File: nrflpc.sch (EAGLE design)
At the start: 71 parts, among them IC1 LPC1111/12/13/14-HVQFN33, IC2 LT1763CS8-3.3, IC3 LM3401, IC5 LM3401, IC6 LM3401, IC7 LM3401, IC8 78L05SMD, Q1 20MHz, Q2 MOSFET-PCHANNEL, Q3 MOSFET-PCHANNEL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

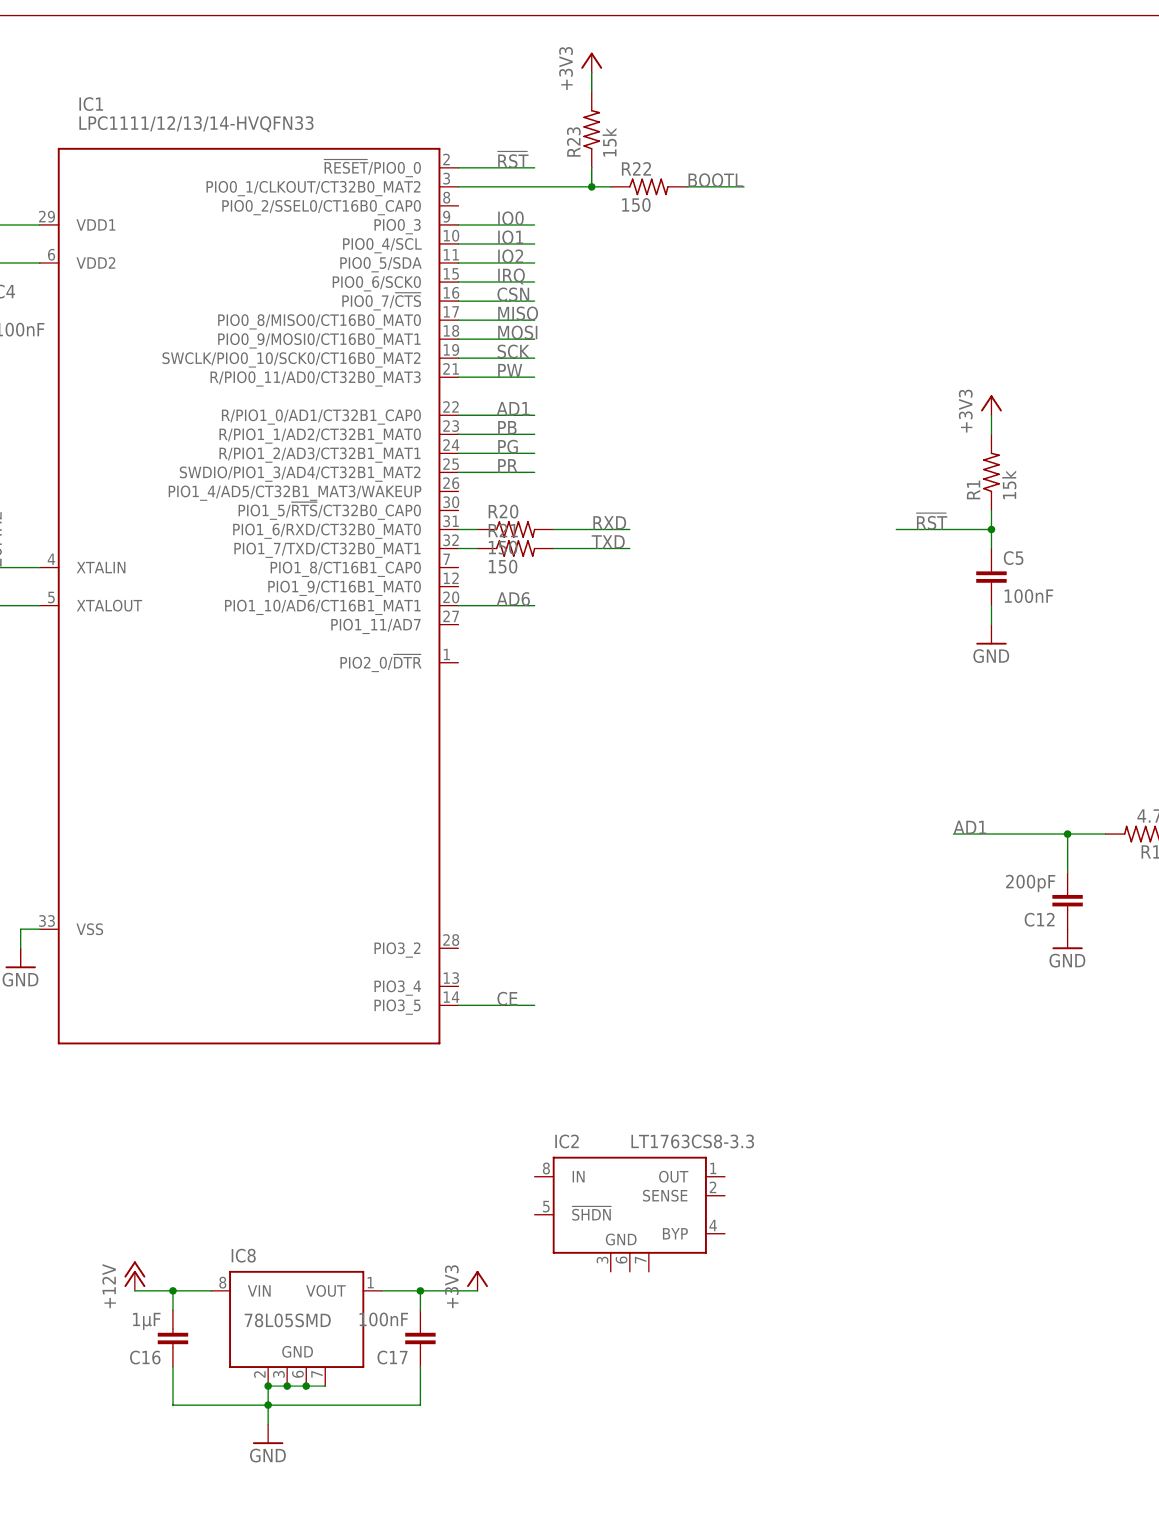
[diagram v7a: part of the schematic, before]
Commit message: Removed unnecessary pullups, new 3.3V regulator, begin routing
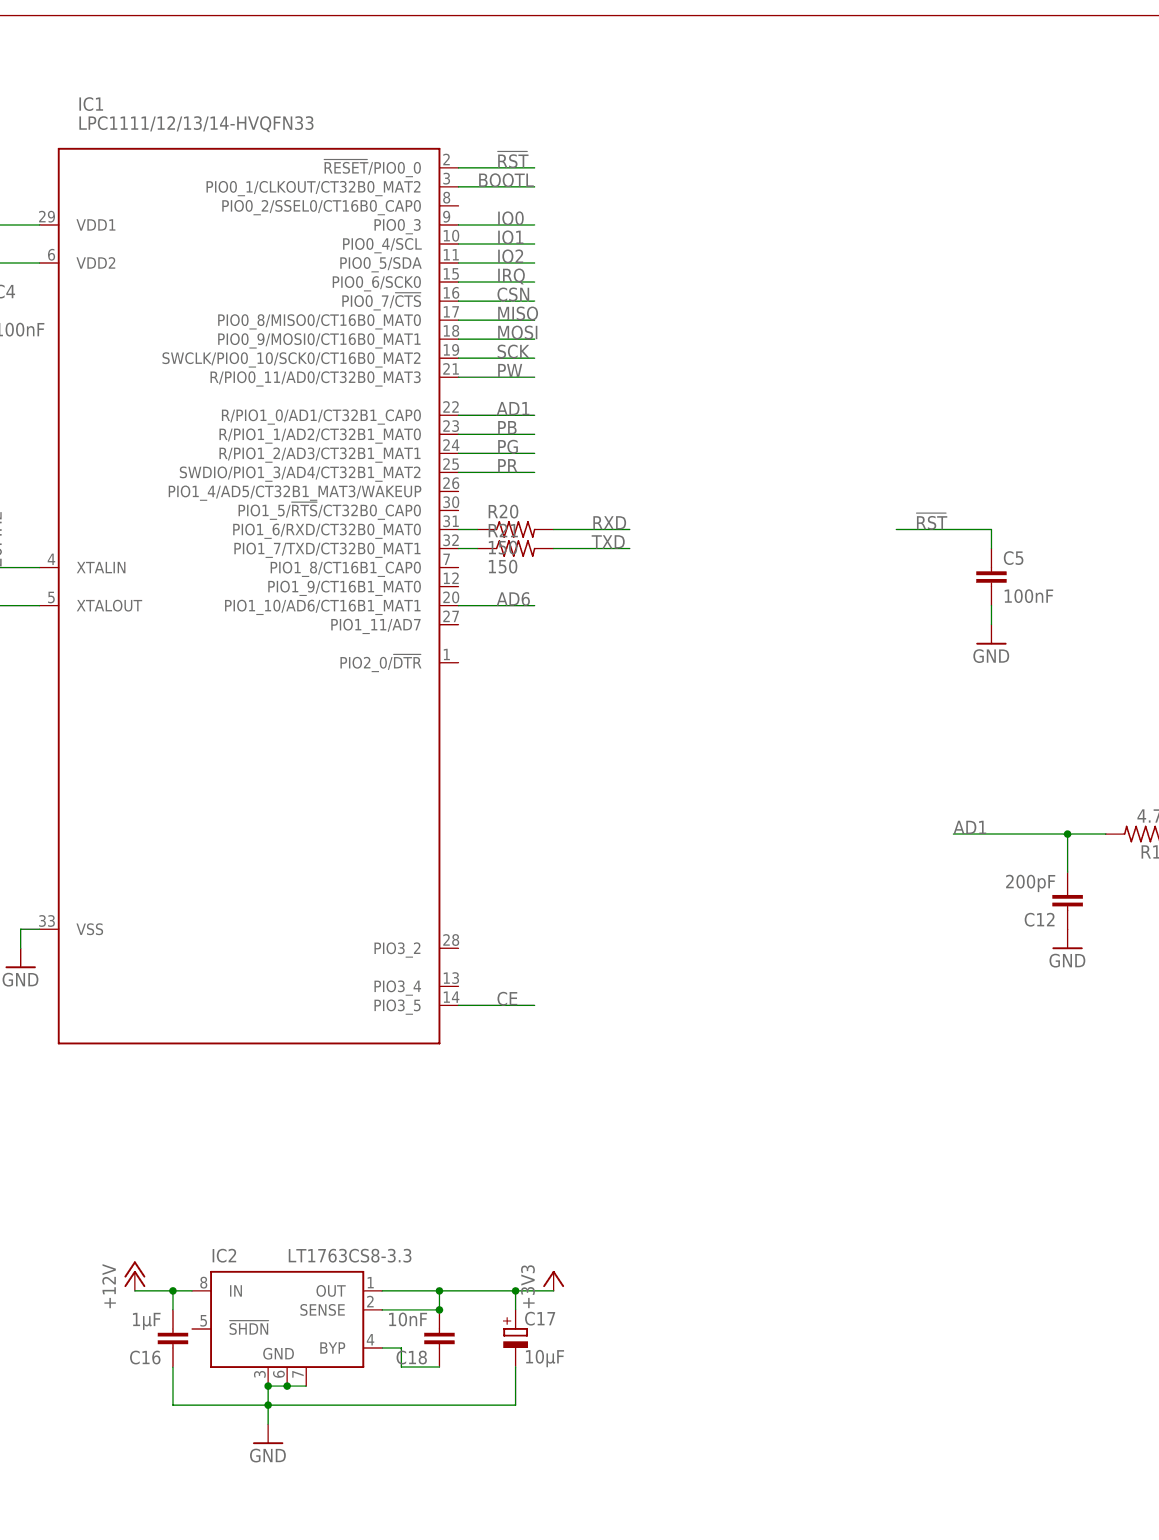
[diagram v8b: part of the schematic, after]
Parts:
- removed IC8: 78L05SMD, linear:78L05SMD
- removed R1, R23: 15k, rcl:R-US_R0402
- removed R22: 150, rcl:R-US_R0402
- added C18: 10nF, SparkFun:CAP0402-CAP
- C17: value 100nF -> 10µF; device SparkFun:CAP0402-CAP -> rcl:CPOL-EUSMCA
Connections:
- net !RST: no longer R1.1
- net +12V: now also IC2.IN; no longer IC8G$1.VIN
- net +3V3: now also C17.+, C18.2, IC2.OUT, IC2.SENSE; no longer C17.2, IC8G$1.VOUT, R1.2, R23.2
- net BOOTL: now also IC1.PIO0_1/CLKOUT/CT32B0_MAT2; no longer R22.2
- net GND: now also C17.-, IC2.GND@1, IC2.GND@2, IC2.GND@3; no longer C17.1, IC8G$1.GND@1, IC8G$1.GND@2, IC8G$1.GND@3, IC8G$1.GND@4
- net N$18: now also C18.1, IC2.BYP; no longer IC1.PIO0_1/CLKOUT/CT32B0_MAT2, R22.1, R23.1
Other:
- moved on the sheet: IC2
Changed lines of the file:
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@@
 <part name="B-" library="solpad" deviceset="SE14" device=""/>
 <part name="C15" library="SparkFun" deviceset="CAP" device="0805" value="1µF"/>
-<part name="IC8" library="linear" deviceset="78L*SMD" device="" technology="05"/>
 <part name="GND11" library="supply1" deviceset="GND" device=""/>
 <part name="C16" library="SparkFun" deviceset="CAP" device="0805" value="1µF"/>
-<part name="C17" library="SparkFun" deviceset="CAP" device="0402-CAP" value="100nF"/>
 <part name="+3V1" library="supply1" deviceset="+3V3" device=""/>
 <part name="FTDI" library="pinhead" deviceset="PINHD-1X4" device=""/>
@@
 <part name="C4" library="rcl" deviceset="C-EU" device="C0402" value="100nF"/>
 <part name="GND5" library="supply1" deviceset="GND" device=""/>
-<part name="R1" library="rcl" deviceset="R-US_" device="R0402" value="15k"/>
-<part name="+3V5" library="supply1" deviceset="+3V3" device=""/>
 <part name="GND13" library="supply1" deviceset="GND" device=""/>
 <part name="C5" library="rcl" deviceset="C-EU" device="C0402" value="100nF"/>
@@
 <part name="R21" library="rcl" deviceset="R-US_" device="R0402" value="150"/>
 <part name="IC2" library="linear-technology" deviceset="LT1763CS8" device="" technology="-3.3"/>
-<part name="R22" library="rcl" deviceset="R-US_" device="R0402" value="150"/>
-<part name="R23" library="rcl" deviceset="R-US_" device="R0402" value="15k"/>
-<part name="+3V3" library="supply1" deviceset="+3V3" device=""/>
+<part name="C18" library="SparkFun" deviceset="CAP" device="0402-CAP" value="10nF"/>
+<part name="C17" library="rcl" deviceset="CPOL-EU" device="SMCA" value="10µF"/>
 </parts>
 <sheets>
@@
 <instance part="B-" gate="1" x="398.78" y="-20.32" rot="R270"/>
 <instance part="C15" gate="G$1" x="396.24" y="-15.24" rot="R180"/>
-<instance part="IC8" gate="G$1" x="208.28" y="48.26"/>
 <instance part="GND11" gate="1" x="205.74" y="27.94"/>
 <instance part="C16" gate="G$1" x="193.04" y="43.18" rot="R180"/>
-<instance part="C17" gate="G$1" x="226.06" y="43.18" rot="R180"/>
-<instance part="+3V1" gate="G$1" x="233.68" y="50.8"/>
+<instance part="+3V1" gate="G$1" x="243.84" y="50.8"/>
 <instance part="FTDI" gate="A" x="88.9" y="139.7"/>
 <instance part="GND8" gate="1" x="73.66" y="134.62"/>
@@
 <instance part="C4" gate="G$1" x="167.64" y="180.34"/>
 <instance part="GND5" gate="1" x="162.56" y="170.18"/>
-<instance part="R1" gate="G$1" x="302.26" y="157.48" rot="R90"/>
-<instance part="+3V5" gate="G$1" x="302.26" y="167.64"/>
 <instance part="GND13" gate="1" x="302.26" y="134.62"/>
 <instance part="C5" gate="G$1" x="302.26" y="144.78"/>
@@
 <instance part="R20" gate="G$1" x="238.76" y="149.86"/>
 <instance part="R21" gate="G$1" x="238.76" y="147.32"/>
-<instance part="IC2" gate="G$1" x="254" y="60.96"/>
-<instance part="R22" gate="G$1" x="256.54" y="195.58"/>
-<instance part="R23" gate="G$1" x="248.92" y="203.2" rot="R90"/>
-<instance part="+3V3" gate="G$1" x="248.92" y="213.36"/>
+<instance part="IC2" gate="G$1" x="208.28" y="45.72"/>
+<instance part="C18" gate="G$1" x="228.6" y="43.18" rot="R180"/>
+<instance part="C17" gate="G$1" x="238.76" y="43.18"/>
 </instances>
 <busses>
@@
 </segment>
 <segment>
-<wire x1="213.36" y1="35.56" x2="210.82" y2="35.56" width="0.1524" layer="91"/>
-<wire x1="210.82" y1="35.56" x2="208.28" y2="35.56" width="0.1524" layer="91"/>
-<wire x1="208.28" y1="35.56" x2="205.74" y2="35.56" width="0.1524" layer="91"/>
-<wire x1="205.74" y1="35.56" x2="205.74" y2="33.02" width="0.1524" layer="91"/>
 <wire x1="205.74" y1="33.02" x2="205.74" y2="30.48" width="0.1524" layer="91"/>
-<wire x1="226.06" y1="38.1" x2="226.06" y2="33.02" width="0.1524" layer="91"/>
-<wire x1="226.06" y1="33.02" x2="205.74" y2="33.02" width="0.1524" layer="91"/>
 <wire x1="205.74" y1="33.02" x2="193.04" y2="33.02" width="0.1524" layer="91"/>
 <wire x1="193.04" y1="33.02" x2="193.04" y2="38.1" width="0.1524" layer="91"/>
-<junction x="210.82" y="35.56"/>
+<pinref part="GND11" gate="1" pin="GND"/>
+<pinref part="C16" gate="G$1" pin="1"/>
+<wire x1="238.76" y1="33.02" x2="205.74" y2="33.02" width="0.1524" layer="91"/>
+<junction x="205.74" y="33.02"/>
+<wire x1="238.76" y1="33.02" x2="238.76" y2="38.1" width="0.1524" layer="91"/>
+<pinref part="IC2" gate="G$1" pin="GND@1"/>
+<wire x1="205.74" y1="35.56" x2="205.74" y2="33.02" width="0.1524" layer="91"/>
+<pinref part="IC2" gate="G$1" pin="GND@2"/>
+<wire x1="205.74" y1="35.56" x2="208.28" y2="35.56" width="0.1524" layer="91"/>
+<junction x="205.74" y="35.56"/>
+<pinref part="IC2" gate="G$1" pin="GND@3"/>
+<wire x1="208.28" y1="35.56" x2="210.82" y2="35.56" width="0.1524" layer="91"/>
 <junction x="208.28" y="35.56"/>
-<junction x="205.74" y="35.56"/>
-<junction x="205.74" y="33.02"/>
-<pinref part="IC8" gate="G$1" pin="GND@4"/>
-<pinref part="IC8" gate="G$1" pin="GND@3"/>
-<pinref part="IC8" gate="G$1" pin="GND@2"/>
-<pinref part="IC8" gate="G$1" pin="GND@1"/>
-<pinref part="GND11" gate="1" pin="GND"/>
-<pinref part="C17" gate="G$1" pin="1"/>
-<pinref part="C16" gate="G$1" pin="1"/>
+<pinref part="C17" gate="G$1" pin="-"/>
 </segment>
 <segment>
@@
 </segment>
 <segment>
-<pinref part="R1" gate="G$1" pin="1"/>
 <pinref part="C5" gate="G$1" pin="1"/>
 <wire x1="302.26" y1="147.32" x2="302.26" y2="149.86" width="0.1524" layer="91"/>
-<wire x1="302.26" y1="149.86" x2="302.26" y2="152.4" width="0.1524" layer="91"/>
 <wire x1="302.26" y1="149.86" x2="289.56" y2="149.86" width="0.1524" layer="91"/>
-<junction x="302.26" y="149.86"/>
 <label x="292.1" y="149.86" size="1.778" layer="95"/>
 </segment>
@@
 </segment>
 <segment>
-<wire x1="187.96" y1="48.26" x2="193.04" y2="48.26" width="0.1524" layer="91"/>
+<pinref part="IC2" gate="G$1" pin="IN"/>
+<pinref part="P+6" gate="1" pin="+12V"/>
+<wire x1="195.58" y1="48.26" x2="193.04" y2="48.26" width="0.1524" layer="91"/>
+<pinref part="C16" gate="G$1" pin="2"/>
+<wire x1="193.04" y1="48.26" x2="187.96" y2="48.26" width="0.1524" layer="91"/>
 <wire x1="193.04" y1="45.72" x2="193.04" y2="48.26" width="0.1524" layer="91"/>
-<pinref part="C16" gate="G$1" pin="2"/>
-<pinref part="P+6" gate="1" pin="+12V"/>
-<pinref part="IC8" gate="G$1" pin="VIN"/>
-<wire x1="198.12" y1="48.26" x2="193.04" y2="48.26" width="0.1524" layer="91"/>
 <junction x="193.04" y="48.26"/>
 </segment>
@@
 <net name="+3V3" class="0">
 <segment>
-<wire x1="233.68" y1="48.26" x2="226.06" y2="48.26" width="0.1524" layer="91"/>
-<wire x1="226.06" y1="48.26" x2="220.98" y2="48.26" width="0.1524" layer="91"/>
-<wire x1="226.06" y1="45.72" x2="226.06" y2="48.26" width="0.1524" layer="91"/>
-<junction x="226.06" y="48.26"/>
-<pinref part="IC8" gate="G$1" pin="VOUT"/>
-<pinref part="C17" gate="G$1" pin="2"/>
+<wire x1="243.84" y1="48.26" x2="238.76" y2="48.26" width="0.1524" layer="91"/>
+<wire x1="238.76" y1="48.26" x2="228.6" y2="48.26" width="0.1524" layer="91"/>
+<wire x1="228.6" y1="48.26" x2="220.98" y2="48.26" width="0.1524" layer="91"/>
 <pinref part="+3V1" gate="G$1" pin="+3V3"/>
+<pinref part="IC2" gate="G$1" pin="OUT"/>
+<pinref part="C18" gate="G$1" pin="2"/>
+<pinref part="IC2" gate="G$1" pin="SENSE"/>
+<wire x1="228.6" y1="45.72" x2="220.98" y2="45.72" width="0.1524" layer="91"/>
+<wire x1="228.6" y1="45.72" x2="228.6" y2="48.26" width="0.1524" layer="91"/>
+<junction x="228.6" y="45.72"/>
+<junction x="228.6" y="48.26"/>
+<wire x1="238.76" y1="45.72" x2="238.76" y2="48.26" width="0.1524" layer="91"/>
+<junction x="238.76" y="48.26"/>
+<pinref part="C17" gate="G$1" pin="+"/>
 </segment>
 <segment>
@@
 <junction x="167.64" y="185.42"/>
 </segment>
-<segment>
-<pinref part="R1" gate="G$1" pin="2"/>
-<pinref part="+3V5" gate="G$1" pin="+3V3"/>
-<wire x1="302.26" y1="165.1" x2="302.26" y2="162.56" width="0.1524" layer="91"/>
-</segment>
-<segment>
-<pinref part="+3V3" gate="G$1" pin="+3V3"/>
-<pinref part="R23" gate="G$1" pin="2"/>
-<wire x1="248.92" y1="210.82" x2="248.92" y2="208.28" width="0.1524" layer="91"/>
-</segment>
 </net>
 <net name="CE" class="0">
@@
 </segment>
 </net>
+<net name="BOOTL" class="0">
+<segment>
+<label x="233.68" y="195.58" size="1.778" layer="95"/>
+<pinref part="IC1" gate="G$1" pin="PIO0_1/CLKOUT/CT32B0_MAT2"/>
+<wire x1="231.14" y1="195.58" x2="241.3" y2="195.58" width="0.1524" layer="91"/>
+</segment>
+</net>
 <net name="N$18" class="0">
 <segment>
-<pinref part="IC1" gate="G$1" pin="PIO0_1/CLKOUT/CT32B0_MAT2"/>
-<wire x1="231.14" y1="195.58" x2="248.92" y2="195.58" width="0.1524" layer="91"/>
-<pinref part="R22" gate="G$1" pin="1"/>
-<pinref part="R23" gate="G$1" pin="1"/>
-<wire x1="248.92" y1="195.58" x2="251.46" y2="195.58" width="0.1524" layer="91"/>
-<wire x1="248.92" y1="198.12" x2="248.92" y2="195.58" width="0.1524" layer="91"/>
-<junction x="248.92" y="195.58"/>
-</segment>
-</net>
-<net name="BOOTL" class="0">
-<segment>
-<pinref part="R22" gate="G$1" pin="2"/>
-<wire x1="261.62" y1="195.58" x2="269.24" y2="195.58" width="0.1524" layer="91"/>
-<label x="261.62" y="195.58" size="1.778" layer="95"/>
-</segment>
-</net>
+<pinref part="IC2" gate="G$1" pin="BYP"/>
+<wire x1="220.98" y1="40.64" x2="223.52" y2="40.64" width="0.1524" layer="91"/>
+<wire x1="223.52" y1="40.64" x2="223.52" y2="38.1" width="0.1524" layer="91"/>
+<pinref part="C18" gate="G$1" pin="1"/>
+<wire x1="223.52" y1="38.1" x2="228.6" y2="38.1" width="0.1524" layer="91"/>
+</segment>
+</net>
